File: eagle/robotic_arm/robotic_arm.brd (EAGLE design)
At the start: 81.3 x 66 mm, 116 parts, among them J2 (ID,OD)=(2.1,5.5)MM, SW1 5A/28V, Y1 16MHz

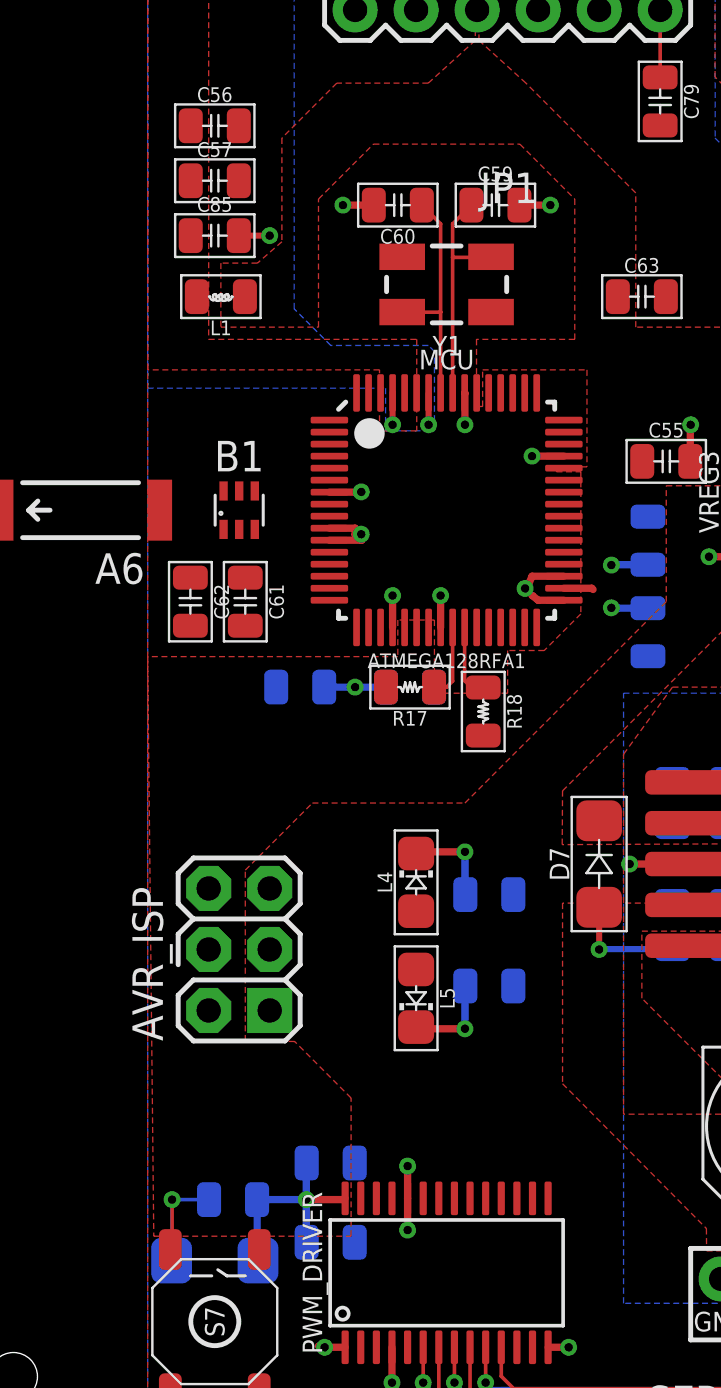
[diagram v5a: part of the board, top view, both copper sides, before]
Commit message: Added tRestrict under crystal oscillator to reduce any potential noise to device
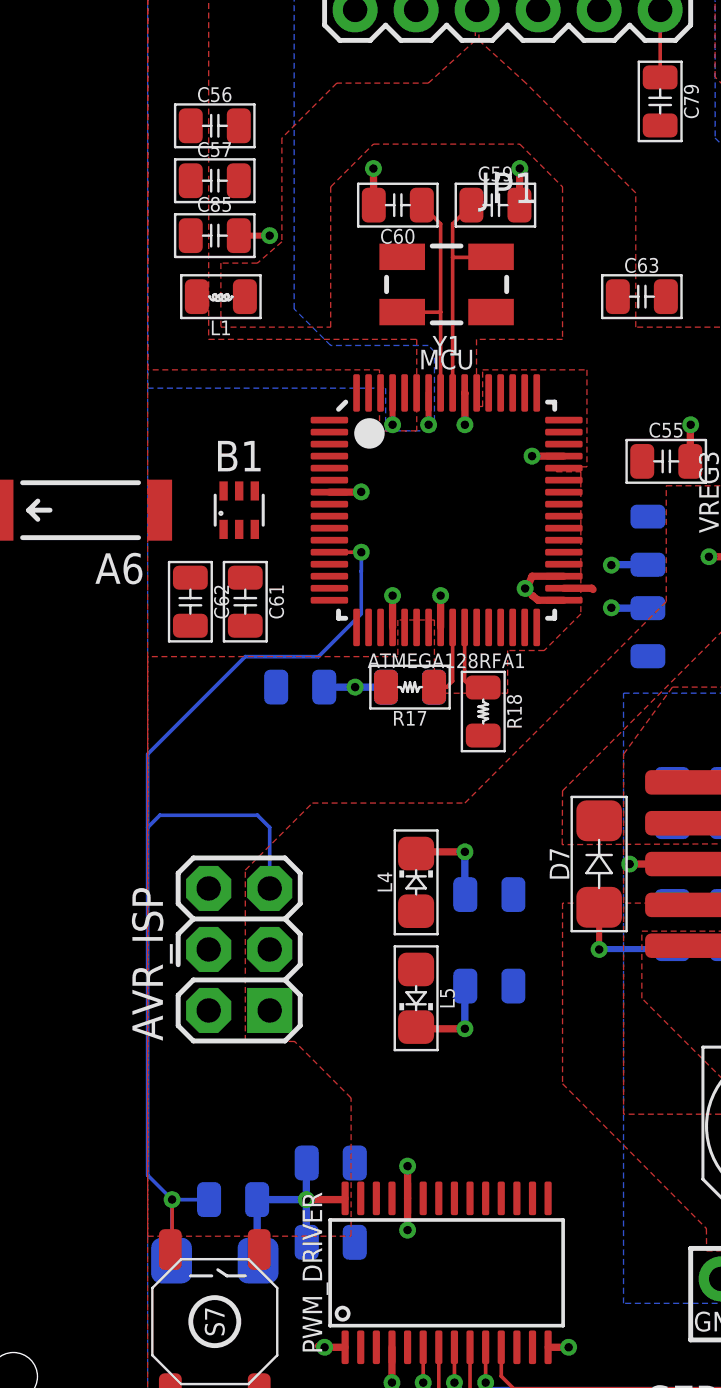
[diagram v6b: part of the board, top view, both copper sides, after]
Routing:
- net RESET: track 6.19 -> 48.4 mm, vias 1 -> 2
- net GND: track 26.2 -> 23.5 mm, vias 16 -> 15
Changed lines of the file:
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@@
 <rectangle x1="26.67" y1="31.242" x2="27.432" y2="31.496" layer="41"/>
 <rectangle x1="15.24" y1="4.318" x2="16.256" y2="6.096" layer="42"/>
+<polygon width="0.1524" layer="41">
+<vertex x="18.288" y="48.768"/>
+<vertex x="19.812" y="50.292"/>
+<vertex x="25.4" y="50.292"/>
+<vertex x="26.924" y="48.768"/>
+<vertex x="26.924" y="43.18"/>
+<vertex x="18.288" y="43.18"/>
+</polygon>
 </plain>
 <attributes>
@@
 <contactref element="R3" pad="1"/>
 <contactref element="R2" pad="1"/>
-<wire x1="19.574" y1="48.26" x2="18.288" y2="48.26" width="0.3048" layer="1"/>
-<via x="18.288" y="48.26" extent="1-16" drill="0.35"/>
-<wire x1="25.638" y1="48.26" x2="26.924" y2="48.26" width="0.3048" layer="1"/>
-<via x="26.924" y="48.26" extent="1-16" drill="0.35"/>
+<wire x1="19.574" y1="48.26" x2="19.558" y2="49.784" width="0.3048" layer="1"/>
+<via x="19.558" y="49.784" extent="1-16" drill="0.35"/>
+<wire x1="25.638" y1="48.26" x2="25.654" y2="49.784" width="0.3048" layer="1"/>
+<via x="25.654" y="49.784" extent="1-16" drill="0.35"/>
 <wire x1="23.356" y1="40.441" x2="23.368" y2="40.429" width="0.3048" layer="1"/>
 <wire x1="23.368" y1="40.429" x2="23.368" y2="39.116" width="0.3048" layer="1"/>
@@
 <wire x1="22.356" y1="30.679" x2="22.356" y2="32.004" width="0.3048" layer="1"/>
 <via x="22.356" y="32.004" extent="1-16" drill="0.35"/>
-<wire x1="17.725" y1="34.81" x2="18.796" y2="34.81" width="0.3048" layer="1"/>
-<wire x1="18.796" y1="34.81" x2="18.796" y2="34.544" width="0.3048" layer="1"/>
-<wire x1="19.05" y1="34.56" x2="18.796" y2="34.544" width="0.3048" layer="1"/>
-<via x="19.05" y="34.56" extent="1-16" drill="0.35"/>
-<wire x1="17.725" y1="34.31" x2="19.07" y2="34.31" width="0.3048" layer="1"/>
-<wire x1="19.07" y1="34.31" x2="19.05" y2="34.56" width="0.3048" layer="1"/>
 <wire x1="17.725" y1="36.31" x2="19.038" y2="36.31" width="0.3048" layer="1"/>
 <wire x1="19.038" y1="36.31" x2="19.05" y2="36.322" width="0.3048" layer="1"/>
@@
 <vertex x="20.574" y="29.464"/>
 <vertex x="10.16" y="29.464"/>
-<vertex x="10.414" y="5.3336"/>
+<vertex x="10.16" y="5.3336"/>
 <vertex x="18.628603125" y="5.33435"/>
 <vertex x="18.628603125" y="11.089121875"/>
@@
 <vertex x="13.208" y="45.847"/>
 <vertex x="13.208" y="43.18"/>
-<vertex x="17.272" y="43.18"/>
-<vertex x="17.272" y="48.514"/>
+<vertex x="17.78" y="43.18"/>
+<vertex x="17.78" y="49.022"/>
 <vertex x="19.558" y="50.8"/>
 <vertex x="25.654" y="50.8"/>
-<vertex x="27.94" y="48.514"/>
-<vertex x="27.94" y="42.672"/>
+<vertex x="27.432" y="49.022"/>
+<vertex x="27.432" y="42.672"/>
 <vertex x="23.8506" y="42.672"/>
 <vertex x="23.8506" y="39.878"/>
@@
 <contactref element="D1" pad="A"/>
 <wire x1="11.154" y1="4.318" x2="11.176" y2="5.102" width="0.1524" layer="16"/>
-<wire x1="11.176" y1="6.858" x2="11.176" y2="5.102" width="0.1524" layer="16"/>
+<wire x1="11.176" y1="5.102" x2="11.176" y2="6.858" width="0.1524" layer="16"/>
 <via x="11.176" y="6.858" extent="1-16" drill="0.35"/>
 <wire x1="12.716" y1="6.858" x2="11.176" y2="6.858" width="0.1524" layer="16"/>
 <wire x1="11.104" y1="4.778" x2="11.176" y2="4.85" width="0.1524" layer="1"/>
 <wire x1="11.176" y1="4.85" x2="11.176" y2="6.858" width="0.1524" layer="1"/>
-<wire x1="17.725" y1="33.81" x2="31.496" y2="51.578" width="0" layer="19" extent="1-1"/>
-<wire x1="15.24" y1="19.812" x2="17.725" y2="33.81" width="0" layer="19" extent="1-1"/>
-<wire x1="12.716" y1="6.858" x2="15.24" y2="19.812" width="0" layer="19" extent="16-16"/>
+<wire x1="11.176" y1="6.858" x2="10.16" y2="7.874" width="0.1524" layer="16"/>
+<wire x1="10.16" y1="7.874" x2="10.16" y2="22.352" width="0.1524" layer="16"/>
+<wire x1="10.668" y1="22.86" x2="10.16" y2="22.352" width="0.1524" layer="16"/>
+<wire x1="15.24" y1="19.812" x2="15.24" y2="22.352" width="0.1524" layer="16"/>
+<wire x1="15.24" y1="22.352" x2="14.732" y2="22.86" width="0.1524" layer="16"/>
+<wire x1="14.732" y1="22.86" x2="10.668" y2="22.86" width="0.1524" layer="16"/>
+<wire x1="10.16" y1="22.352" x2="10.16" y2="25.4" width="0.1524" layer="16"/>
+<wire x1="10.16" y1="25.4" x2="14.224" y2="29.464" width="0.1524" layer="16"/>
+<wire x1="17.272" y1="29.464" x2="19.05" y2="31.242" width="0.1524" layer="16"/>
+<wire x1="19.05" y1="31.242" x2="19.05" y2="33.02" width="0.1524" layer="16"/>
+<wire x1="14.224" y1="29.464" x2="17.272" y2="29.464" width="0.1524" layer="16"/>
+<wire x1="19.05" y1="33.02" x2="19.05518125" y2="33.02518125" width="0.1524" layer="16"/>
+<wire x1="19.05518125" y1="33.02518125" x2="19.05518125" y2="33.81" width="0.1524" layer="16"/>
+<via x="19.05518125" y="33.81" extent="1-16" drill="0.35"/>
+<wire x1="17.725" y1="33.81" x2="19.05518125" y2="33.81" width="0.1524" layer="1"/>
+<wire x1="19.05518125" y1="33.81" x2="31.496" y2="51.578" width="0" layer="19" extent="1-1"/>
 </signal>
 <signal name="N$41">

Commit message: Robotic Arm, Rev 1:  Completed all routes.  Messy as shit.  Much clean up to do
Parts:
- A6: value ANTENNASMD5 -> 2.4GHz/802.11/0.5dBi/3W
- B1: value 748421245 -> Impedence UNBAL/BAL (50Ω/100Ω)
- moved R3 6.48 mm to (19.6, 23.9), turned to 270 degrees
- moved R2 6.48 mm to (19.6, 11.4), turned to 90 degrees
- moved C26 2.65 mm to (48.8, 50.0)
- moved C18 2.65 mm to (48.8, 52.3)
- moved C53 1.48 mm to (32.3, 35.1)
- moved C54 1.30 mm to (32.3, 30.2)
- moved C55 1.08 mm to (32.5, 38.4), turned to 90 degrees
- moved C59 0.51 mm to (24.6, 48.8)
- moved C60 0.51 mm to (20.6, 48.8)
- moved Y1 0.51 mm to (22.6, 45.5)
- moved C52 0.51 mm to (16.5, 27.7)
- moved C58 0.51 mm to (21.1, 27.7)
- moved R17 0.51 mm to (21.1, 27.7)
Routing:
- net A0: track 0.00 -> 92.2 mm, vias 0 -> 2
- net SSN: track 0.00 -> 58.7 mm, vias 0 -> 4
- net PE7: track 0.00 -> 52.8 mm, vias 0 -> 4
- net PE6: track 0.00 -> 49.4 mm, vias 0 -> 2
- net RESET: track 48.4 -> 96.6 mm, vias 2 -> 3
- net PE2: track 0.00 -> 44.2 mm, vias 0 -> 4
- net MOSI: track 0.00 -> 40.3 mm, vias 0 -> 1
- net PB6: track 0.00 -> 36.7 mm, vias 0 -> 2
- net PB7: track 0.00 -> 36.1 mm, vias 0 -> 2
- net MISO: track 0.00 -> 31.7 mm, vias 0 -> 1
- net SCK: track 0.00 -> 28.5 mm, vias 0 -> 1
- net SDA: track 3.11 -> 28.4 mm, vias 0 -> 2
- net SCL: track 3.33 -> 27.9 mm, vias 0 -> 2
- net RX0: track 0.00 -> 22.2 mm, vias 0 -> 2
- net TX0: track 0.00 -> 19.7 mm, vias 0 -> 1
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
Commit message: Rev 1: Board complete.  Sent to Fab
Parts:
- removed C56: 0.1uF/50V, MrSwirlyEyes:CAP_CER_SMD-805
- removed C84: 100UF/16V, MrSwirlyEyes:CAP_POL_SMD_L6.6-W6.6
- removed J2: (ID,OD)=(2.1,5.5)MM, MrSwirlyEyes:POWER_JACK_SLOT_ID2.1MM-OD5.5MM
- removed SUPPLY51, SUPPLY52: 2PT_GND_TIE, SparkFun-PowerSymbols:2PT_GND_TIE
- added ANALOG_BR, NOISE_BR: 2PT_GND_TIE, PiB_power_symbols:2PT_GND_TIE
- added C21, C23, C24: 1uF/25V, PiB_capacitors:_CER_SMD-805
- added C22: 0.1uF/50V, PiB_capacitors:_CER_SMD-805
- added J1: (ID,OD)=(2.1,5.5)MM, PiB_connectors:POWER_JACK_SLOT_ID2.1MM-OD5.5MM
- A6: device lib_kenmei:ANTENNA-CHIP5 -> PiB_radio_frequency:ANTENNA-CHIP5
- AVR_ISP: device MrSwirlyEyes:2X3-NS -> PiB_connectors:2X3-NS
- B1: device lib_kenmei:0805_BALUN -> PiB_radio_frequency:0805_BALUN
- BATT1: device MrSwirlyEyes:DUAL_PTH_PADS -> PiB:DUAL_PTH_PADS
- C1, C10, C12, C14, C16, C18, C19, C25, C26, C3, C4, C47, C48, C49, C5, C50, C51, C52, C53, C54, C55, C57, C58, C59, C6, C60, C61, C62, C63, C7, C79, C8, C81, C82, C83, C92, C93, C94, C95, C96, C97, C98: device MrSwirlyEyes:CAP_CER_SMD-805 -> PiB_capacitors:_CER_SMD-805
- C11, C13, C15, C17, C2, C9: value 100UF/16V -> 10uF/20V; device MrSwirlyEyes:CAP_POL_SMD_L6.6-W6.6 -> PiB_capacitors:_TANT_SMD-1206
- C20: value 220uF/16V -> 100UF/16V; device MrSwirlyEyes:CAP_POL_SMD_L6.6-W6.6 -> PiB_capacitors:_AE_SMD_L6.6-W6.6
- C80: device MrSwirlyEyes:CAP_POL_SMD_L6.6-W6.6 -> PiB_capacitors:_AE_SMD_L6.6-W6.6
- C85: value 1uF/25V -> 0.1uF/50V; device MrSwirlyEyes:CAP_CER_SMD-805 -> PiB_capacitors:_CER_SMD-805
- D1, D6, D7: device MrSwirlyEyes:DIODE_SMD_1A-50V-SOD123F -> PiB_discrete_semiconductors:SOD123F
- DEMUX1: device MrSwirlyEyes:SSOP-24 -> PiB:SSOP-24
- FSR_INDEX, FSR_MIDDLE, FSR_PINKY, FSR_RING, FSR_THUMB: device MrSwirlyEyes:CONNECTOR_FSR -> PiB:CONNECTOR_FSR
- JP1: device MrSwirlyEyes:FTDI_BASIC-6PIN-MALE-RA -> PiB_connectors:FTDI_BASIC-6PIN-MALE-RA
- L1, L2: device MrSwirlyEyes:INDUCTOR_SMD-805 -> PiB_inductors:_SMD-805
- L3, L4, L5: device MrSwirlyEyes:LED_SMD-805_ -> PiB_leds:LED_SMD-805_
- MCU: device MrSwirlyEyes:VFQFN-64 -> PiB_ic_microcontrollers:VFQFN-64
- PWM_DRIVER: device MrSwirlyEyes:TSSOP-28 -> PiB:TSSOP-28
- R1, R10, R11, R12, R13, R14, R15, R16, R17, R18, R2, R3, R39, R4, R40, R41, R42, R43, R5, R6, R7, R8, R9: device MrSwirlyEyes:RESISTOR_SMD-805 -> PiB_resistors:RESISTOR_SMD-805
- S7: device MrSwirlyEyes:SW_MOMENTARY_SPST-NO_SMD_12V_50MA_5.2MM -> PiB_switches:BTN_MOMENTARY_SPST-NO_SMD_12V_50MA_L5.2-W5.2
- SERVO_INDEX, SERVO_MIDDLE, SERVO_PINKY, SERVO_RING, SERVO_THUMB, SERVO_WRIST: device MrSwirlyEyes:CONNECTOR_SERVO -> PiB:CONNECTOR_SERVO
- SW1: device MrSwirlyEyes:SW-SLIDE_SPDT_5A-28V_13L-7W -> PiB_switches:SW_TOGGLE_SPDT_5A-28V_13L-7W
- TEMP_INDEX, TEMP_MIDDLE, TEMP_PINKY, TEMP_RING, TEMP_THUMB: device MrSwirlyEyes:CONNECTOR_TMP36 -> PiB:CONNECTOR_TMP36
- VREG1: device MrSwirlyEyes:TO-263-5 -> PiB_ic_power:TO-263-5
- VREG3: device MrSwirlyEyes:SOIC-8_W3.9MM -> PiB_ic_power:SOIC-8_W3.9MM
- Y1: device MrSwirlyEyes:CRYSTAL-SMD-5X3 -> PiB:CRYSTAL-SMD-5X3
- moved C20 22.4 mm to (38.6, 18.5), turned to 180 degrees
- moved C98 18.2 mm to (50.0, 25.9), flipped to the top, turned to 180 degrees
- moved C95 18.0 mm to (53.3, 36.1), flipped to the top, turned to 90 degrees
- moved VREG1 17.5 mm to (59.7, 20.3)
- moved R3 16.8 mm to (27.7, 9.14), flipped to the top, turned to 180 degrees
- moved C97 16.5 mm to (50.0, 28.2), flipped to the top, turned to 180 degrees
- moved D7 15.8 mm to (44.7, 22.4)
- moved C96 15.3 mm to (51.1, 36.1), flipped to the top, turned to 90 degrees
- moved L3 13.6 mm to (58.7, 32.5)
- moved R1 13.6 mm to (58.7, 36.8)
- moved C18 13.1 mm to (39.4, 43.2), flipped to the top, turned to 90 degrees
- moved C83 12.7 mm to (44.7, 17.5), flipped to the top, turned to 270 degrees
- moved C94 12.7 mm to (47.0, 17.5), flipped to the top, turned to 270 degrees
- moved L4 11.0 mm to (28.2, 11.4), turned to 180 degrees
- moved C57 9.96 mm to (16.3, 39.9), turned to 90 degrees
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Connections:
- new net N$10: C21.1, MCU.21, MCU.22
- new net N$11: C57.1, MCU.60
- net 5V: now also C11.+, C13.+, C15.+, C17.+, C2.+, C20.A, C9.+; no longer C11.A, C13.A, C15.A, C17.A, C2.A, C9.A
- net A0: no longer DEMUX1.1
- net A5: now also DEMUX1.1
- net AGND: now also ANALOG_BR.P$2, C22.2, C23.2, C24.2; no longer SUPPLY52.P$2
- net AVCC: now also C22.1, C23.1, C24.1; no longer C56.1, C57.1, MCU.60
- net BATT_+: now also J1.PWR, SW1.2; no longer J2.PWR, SW1.P$2
- net BATT_-: now also J1.GND@2; no longer J2.GND@2
- net FSR_INDEX: now also FSR_RING.-, R39.2; no longer FSR_INDEX.-, R41.2
- net FSR_PINKY: now also FSR_THUMB.-, R42.2; no longer FSR_PINKY.-, R16.2
- net FSR_RING: now also FSR_INDEX.-, R41.2; no longer FSR_RING.-, R39.2
- net FSR_THUMB: now also FSR_PINKY.-, R16.2; no longer FSR_THUMB.-, R42.2
- net GND: now also C21.2, J1.GND@1, NOISE_BR.P$2; no longer C20.K, C56.2, C84.K, J2.GND@1, SUPPLY51.P$2
- net N$38: now also ANALOG_BR.P$1; no longer SUPPLY52.P$1
- net NGND: now also C11.-, C13.-, C15.-, C17.-, C2.-, C20.K, C9.-, NOISE_BR.P$1; no longer C11.K, C13.K, C15.K, C17.K, C2.K, C9.K, SUPPLY51.P$1
- net VBATT: now also SW1.1; no longer C20.A, C84.A, SW1.P$1
- net VCC: no longer MCU.21, MCU.22
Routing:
- net AVCC: track 32.2 -> 235.9 mm, vias 2 -> 4
- net 5V: track 22.4 -> 159.8 mm, vias 1 -> 0
- net VCC: track 22.6 -> 144.0 mm, vias 5 -> 6
- net A0: track 92.2 -> 0.00 mm, vias 2 -> 0
- net GND: track 35.2 -> 99.3 mm, vias 37 -> 47
- net A5: track 0.00 -> 43.0 mm, vias 0 -> 2
- net VBATT: track 14.1 -> 56.3 mm, vias 5 -> 0
- net SSN: track 58.7 -> 31.0 mm, vias 4 -> 2
- net PE7: track 52.8 -> 26.3 mm, vias 4 -> 0
- net NGND: track 8.05 -> 34.3 mm, vias 2 -> 54
- net FSR_THUMB: track 39.1 -> 14.0 mm, vias 1 -> 0
- net BATT_+: track 0.00 -> 24.9 mm
- net AGND: track 8.76 -> 31.0 mm, vias 5 -> 25
- net FSR_PINKY: track 19.1 -> 35.3 mm, vias 1 -> 0
- net RESET: track 96.6 -> 81.1 mm, vias 3 -> 4
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- removed copper zone on layer 1, net 5V
- removed copper zone on layer 1, net AVCC
- removed copper zone on layer 1, net BATT_+
- removed copper zone on layer 16, net BATT_-
- removed copper zone on layer 1, net VBATT
- removed copper zone on layer 1, net VCC
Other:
- board size 81.3 x 66 mm -> 81.3 x 61 mm
- board text added: "Designed by: MrSwirlyEyes"
- board text added: "Transmission of Touch VR Robotic Arm Rev 1"
